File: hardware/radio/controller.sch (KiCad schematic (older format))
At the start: 11 parts, among them IC301 ATMEGA328-P, Q301 Q_NMOS_DGS, X301 8MHz

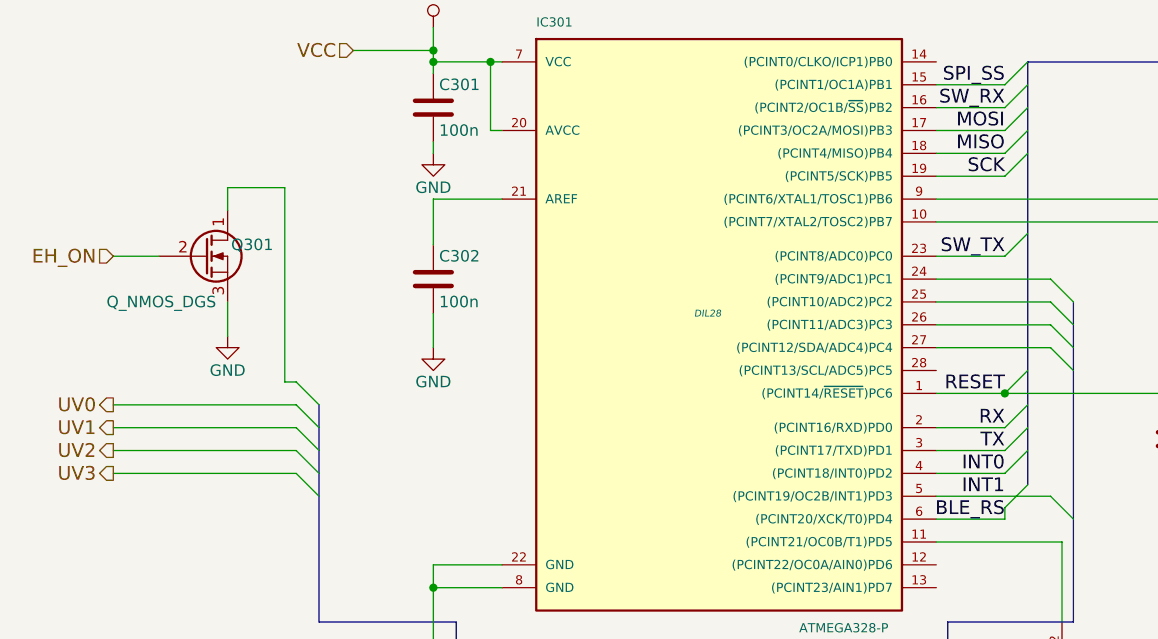
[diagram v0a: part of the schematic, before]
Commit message: Add accelerometer to schematic
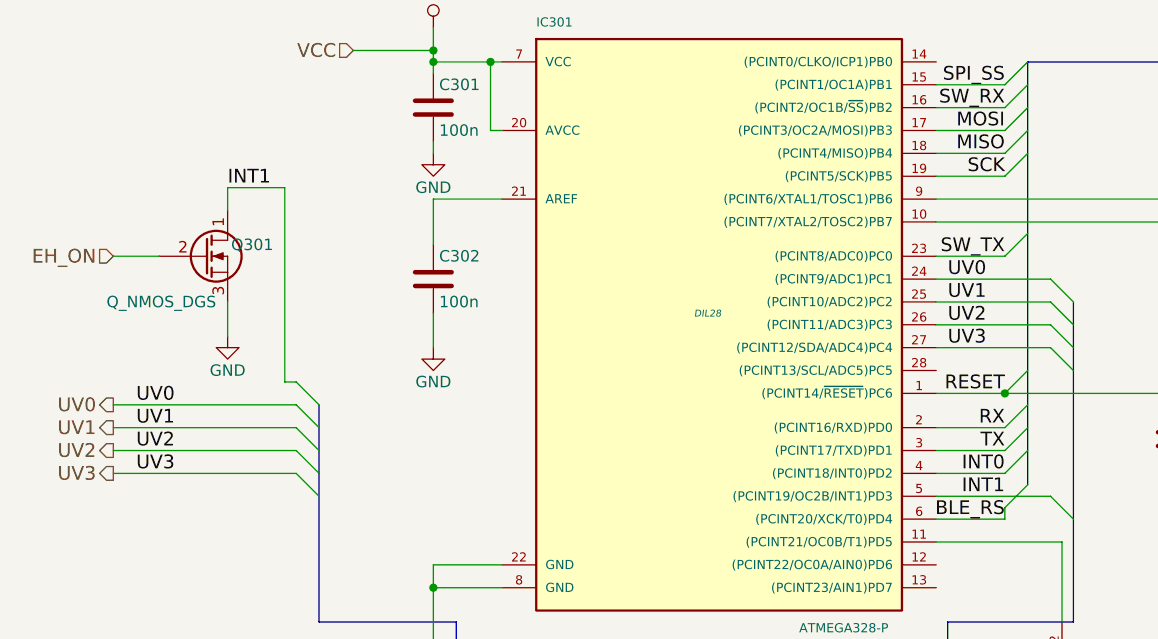
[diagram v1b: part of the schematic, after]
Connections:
- net INT1: now also Q301.1 (D)
- net UV0: now also IC301.24 ((PCINT9/ADC1)PC1)
- net UV1: now also IC301.25 ((PCINT10/ADC2)PC2)
- net UV2: now also IC301.26 ((PCINT11/ADC3)PC3)
- net UV3: now also IC301.27 ((PCINT12/SDA/ADC4)PC4)
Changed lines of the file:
@@
 LIBS:sensors
 LIBS:rfcom
+LIBS:radio-cache
 EELAYER 25 0
 EELAYER END
@@
 $EndComp
 $Comp
-L GND #PWR026
+L GND #PWR308
 U 1 1 55EA8C66
 P 7600 3250
-F 0 "#PWR026" H 7600 3000 50  0001 C CNN
+F 0 "#PWR308" H 7600 3000 50  0001 C CNN
 F 1 "GND" H 7600 3100 50  0000 C CNN
 F 2 "" H 7600 3250 60  0000 C CNN
@@
 $EndComp
 $Comp
-L GND #PWR027
+L GND #PWR307
 U 1 1 55EA8C82
 P 7300 3250
-F 0 "#PWR027" H 7300 3000 50  0001 C CNN
+F 0 "#PWR307" H 7300 3000 50  0001 C CNN
 F 1 "GND" H 7300 3100 50  0000 C CNN
 F 2 "" H 7300 3250 60  0000 C CNN
@@
 $EndComp
 $Comp
-L GND #PWR028
+L GND #PWR306
 U 1 1 55EA8C9E
 P 7000 3250
-F 0 "#PWR028" H 7000 3000 50  0001 C CNN
+F 0 "#PWR306" H 7000 3000 50  0001 C CNN
 F 1 "GND" H 7000 3100 50  0000 C CNN
 F 2 "" H 7000 3250 60  0000 C CNN
@@
 $EndComp
 $Comp
-L VCC #PWR029
+L VCC #PWR303
 U 1 1 55EA9129
 P 6450 3050
-F 0 "#PWR029" H 6450 2900 50  0001 C CNN
+F 0 "#PWR303" H 6450 2900 50  0001 C CNN
 F 1 "VCC" H 6450 3200 50  0000 C CNN
 F 2 "" H 6450 3050 60  0000 C CNN
@@
 $EndComp
 $Comp
-L GND #PWR030
+L GND #PWR309
 U 1 1 55EA91E9
 P 6450 3850
-F 0 "#PWR030" H 6450 3600 50  0001 C CNN
+F 0 "#PWR309" H 6450 3600 50  0001 C CNN
 F 1 "GND" H 6450 3700 50  0000 C CNN
 F 2 "" H 6450 3850 60  0000 C CNN
@@
 TX
 $Comp
-L GND #PWR031
+L GND #PWR310
 U 1 1 55EA9D7E
 P 3200 4750
-F 0 "#PWR031" H 3200 4500 50  0001 C CNN
+F 0 "#PWR310" H 3200 4500 50  0001 C CNN
 F 1 "GND" H 3200 4600 50  0000 C CNN
 F 2 "" H 3200 4750 60  0000 C CNN
@@
 $EndComp
 $Comp
-L GND #PWR032
+L GND #PWR305
 U 1 1 55EA9F10
 P 3200 3250
-F 0 "#PWR032" H 3200 3000 50  0001 C CNN
+F 0 "#PWR305" H 3200 3000 50  0001 C CNN
 F 1 "GND" H 3200 3100 50  0000 C CNN
 F 2 "" H 3200 3250 60  0000 C CNN
@@
 $EndComp
 $Comp
-L VCC #PWR033
+L VCC #PWR301
 U 1 1 55EAA1EE
 P 3200 1850
-F 0 "#PWR033" H 3200 1700 50  0001 C CNN
+F 0 "#PWR301" H 3200 1700 50  0001 C CNN
 F 1 "VCC" H 3200 2000 50  0000 C CNN
 F 2 "" H 3200 1850 60  0000 C CNN
@@
 $EndComp
 $Comp
-L GND #PWR034
+L GND #PWR302
 U 1 1 55EAA376
 P 3200 2400
-F 0 "#PWR034" H 3200 2150 50  0001 C CNN
+F 0 "#PWR302" H 3200 2150 50  0001 C CNN
 F 1 "GND" H 3200 2250 50  0000 C CNN
 F 2 "" H 3200 2400 60  0000 C CNN
@@
 $EndComp
 $Comp
-L GND #PWR035
+L GND #PWR311
 U 1 1 55EACDAA
 P 5950 5400
-F 0 "#PWR035" H 5950 5150 50  0001 C CNN
+F 0 "#PWR311" H 5950 5150 50  0001 C CNN
 F 1 "GND" H 5950 5250 50  0000 C CNN
 F 2 "" H 5950 5400 60  0000 C CNN
@@
 $EndComp
 $Comp
-L GND #PWR036
+L GND #PWR304
 U 1 1 55EAF28A
 P 2300 3200
-F 0 "#PWR036" H 2300 2950 50  0001 C CNN
+F 0 "#PWR304" H 2300 2950 50  0001 C CNN
 F 1 "GND" H 2300 3050 50  0000 C CNN
 F 2 "" H 2300 3200 60  0000 C CNN
@@
 Text Label 9450 900  2    60   ~ 0
 BLE_RS
+Text Label 2300 2550 0    60   ~ 0
+INT1
+Text Label 1900 3500 0    60   ~ 0
+UV0
+Text Label 1900 3600 0    60   ~ 0
+UV1
+Text Label 1900 3700 0    60   ~ 0
+UV2
+Text Label 1900 3800 0    60   ~ 0
+UV3
+Text Label 5450 2950 0    60   ~ 0
+UV0
+Text Label 5450 3050 0    60   ~ 0
+UV1
+Text Label 5450 3150 0    60   ~ 0
+UV2
+Text Label 5450 3250 0    60   ~ 0
+UV3
 $EndSCHEMATC

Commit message: Work on PCB
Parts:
- removed IC301: ATMEGA328-P, DIL28, symbol ATMEGA328-P
- added C?: C, symbol C
- added IC?: ATMEGA328-A, TQFP32, symbol ATMEGA328-A
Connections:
- net BLE_RS: now also IC?.2 ((PCINT20/XCK/T0)PD4)
- net GND: now also C?.2, IC?.21 (GND), IC?.3 (GND), IC?.5 (GND)
- net INT0: now also IC?.32 ((PCINT18/INT0)PD2)
- net INT1: now also IC?.1 ((PCINT19/OC2B/INT1)PD3)
- net MISO: now also IC?.16 ((PCINT4/MISO)PB4)
- net MOSI: now also IC?.15 ((PCINT3/OC2A/MOSI)PB3)
- net RESET: now also IC?.29 ((PCINT14/~RESET~)PC6)
- net RX: now also IC?.30 ((PCINT16/RXD)PD0)
- net SCK: now also IC?.17 ((PCINT5/SCK)PB5)
- net SPI_SS: now also IC?.13 ((PCINT1/OC1A)PB1)
- net SW_RX: now also IC?.14 ((PCINT2/OC1B/~SS~)PB2)
- net SW_TX: now also IC?.23 ((PCINT8/ADC0)PC0)
- net TX: now also IC?.31 ((PCINT17/TXD)PD1)
- net UV0: now also IC?.24 ((PCINT9/ADC1)PC1)
- net UV1: now also IC?.25 ((PCINT10/ADC2)PC2)
- net UV2: now also IC?.26 ((PCINT11/ADC3)PC3)
- net UV3: now also IC?.27 ((PCINT12/SDA/ADC4)PC4)
- net VCC: now also C?.1, IC?.18 (AVCC), IC?.4 (VCC), IC?.6 (VCC)
- net at C304.1, X301.2: now also IC?.8 ((PCINT7/XTAL2/TOSC2)PB7)
- net at D301.2 (A): now also IC?.9 ((PCINT21/OC0B/T1)PD5)
- net at C302.1: now also IC?.20 (AREF)
- net at C303.1, X301.1: now also IC?.7 ((PCINT6/XTAL1/TOSC1)PB6)
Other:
- moved on the sheet: C301
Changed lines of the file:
@@
 $EndDescr
-$Comp
-L ATMEGA328-P IC301
-U 1 1 55EA8691
-P 4400 3100
-F 0 "IC301" H 3650 4350 40  0000 L BNN
-F 1 "ATMEGA328-P" H 4800 1700 40  0000 L BNN
-F 2 "DIL28" H 4400 3100 30  0000 C CIN
-F 3 "" H 4400 3100 60  0000 C CNN
-	1    4400 3100
-	1    0    0    -1
-$EndComp
 $Comp
 L CRYSTAL_SMD X301
@@
 $EndComp
 $Comp
-L GND #PWR308
+L GND #PWR028
 U 1 1 55EA8C66
 P 7600 3250
-F 0 "#PWR308" H 7600 3000 50  0001 C CNN
+F 0 "#PWR028" H 7600 3000 50  0001 C CNN
 F 1 "GND" H 7600 3100 50  0000 C CNN
 F 2 "" H 7600 3250 60  0000 C CNN
@@
 $EndComp
 $Comp
-L GND #PWR307
+L GND #PWR029
 U 1 1 55EA8C82
 P 7300 3250
-F 0 "#PWR307" H 7300 3000 50  0001 C CNN
+F 0 "#PWR029" H 7300 3000 50  0001 C CNN
 F 1 "GND" H 7300 3100 50  0000 C CNN
 F 2 "" H 7300 3250 60  0000 C CNN
@@
 $EndComp
 $Comp
-L GND #PWR306
+L GND #PWR030
 U 1 1 55EA8C9E
 P 7000 3250
-F 0 "#PWR306" H 7000 3000 50  0001 C CNN
+F 0 "#PWR030" H 7000 3000 50  0001 C CNN
 F 1 "GND" H 7000 3100 50  0000 C CNN
 F 2 "" H 7000 3250 60  0000 C CNN
@@
 $EndComp
 $Comp
-L VCC #PWR303
+L VCC #PWR031
 U 1 1 55EA9129
 P 6450 3050
-F 0 "#PWR303" H 6450 2900 50  0001 C CNN
+F 0 "#PWR031" H 6450 2900 50  0001 C CNN
 F 1 "VCC" H 6450 3200 50  0000 C CNN
 F 2 "" H 6450 3050 60  0000 C CNN
@@
 $EndComp
 $Comp
-L GND #PWR309
+L GND #PWR032
 U 1 1 55EA91E9
 P 6450 3850
-F 0 "#PWR309" H 6450 3600 50  0001 C CNN
+F 0 "#PWR032" H 6450 3600 50  0001 C CNN
 F 1 "GND" H 6450 3700 50  0000 C CNN
 F 2 "" H 6450 3850 60  0000 C CNN
@@
 TX
 $Comp
-L GND #PWR310
+L GND #PWR033
 U 1 1 55EA9D7E
 P 3200 4750
-F 0 "#PWR310" H 3200 4500 50  0001 C CNN
+F 0 "#PWR033" H 3200 4500 50  0001 C CNN
 F 1 "GND" H 3200 4600 50  0000 C CNN
 F 2 "" H 3200 4750 60  0000 C CNN
@@
 $EndComp
 $Comp
-L GND #PWR305
+L GND #PWR034
 U 1 1 55EA9F10
 P 3200 3250
-F 0 "#PWR305" H 3200 3000 50  0001 C CNN
+F 0 "#PWR034" H 3200 3000 50  0001 C CNN
 F 1 "GND" H 3200 3100 50  0000 C CNN
 F 2 "" H 3200 3250 60  0000 C CNN
@@
 $EndComp
 $Comp
-L VCC #PWR301
+L VCC #PWR035
 U 1 1 55EAA1EE
-P 3200 1850
-F 0 "#PWR301" H 3200 1700 50  0001 C CNN
-F 1 "VCC" H 3200 2000 50  0000 C CNN
-F 2 "" H 3200 1850 60  0000 C CNN
-F 3 "" H 3200 1850 60  0000 C CNN
-	1    3200 1850
+P 2900 1850
+F 0 "#PWR035" H 2900 1700 50  0001 C CNN
+F 1 "VCC" H 2900 2000 50  0000 C CNN
+F 2 "" H 2900 1850 60  0000 C CNN
+F 3 "" H 2900 1850 60  0000 C CNN
+	1    2900 1850
 	1    0    0    -1
 $EndComp
@@
 L C C301
 U 1 1 55EAA2CA
-P 3200 2200
-F 0 "C301" H 3225 2300 50  0000 L CNN
-F 1 "100n" H 3225 2100 50  0000 L CNN
-F 2 "" H 3238 2050 30  0000 C CNN
-F 3 "" H 3200 2200 60  0000 C CNN
-	1    3200 2200
-	1    0    0    -1
-$EndComp
-$Comp
-L GND #PWR302
+P 2900 2200
+F 0 "C301" H 2925 2300 50  0000 L CNN
+F 1 "100n" H 2925 2100 50  0000 L CNN
+F 2 "" H 2938 2050 30  0000 C CNN
+F 3 "" H 2900 2200 60  0000 C CNN
+	1    2900 2200
+	1    0    0    -1
+$EndComp
+$Comp
+L GND #PWR036
 U 1 1 55EAA376
-P 3200 2400
-F 0 "#PWR302" H 3200 2150 50  0001 C CNN
-F 1 "GND" H 3200 2250 50  0000 C CNN
-F 2 "" H 3200 2400 60  0000 C CNN
-F 3 "" H 3200 2400 60  0000 C CNN
-	1    3200 2400
+P 2900 2400
+F 0 "#PWR036" H 2900 2150 50  0001 C CNN
+F 1 "GND" H 2900 2250 50  0000 C CNN
+F 2 "" H 2900 2400 60  0000 C CNN
+F 3 "" H 2900 2400 60  0000 C CNN
+	1    2900 2400
 	1    0    0    -1
 $EndComp
@@
 Text HLabel 2850 4650 0    60   Input ~ 0
 GND
-Text HLabel 2850 1950 0    60   Input ~ 0
+Text HLabel 2550 1950 0    60   Input ~ 0
 VCC
 $Comp
@@
 $EndComp
 $Comp
-L GND #PWR311
+L GND #PWR037
 U 1 1 55EACDAA
 P 5950 5400
-F 0 "#PWR311" H 5950 5150 50  0001 C CNN
+F 0 "#PWR037" H 5950 5150 50  0001 C CNN
 F 1 "GND" H 5950 5250 50  0000 C CNN
 F 2 "" H 5950 5400 60  0000 C CNN
@@
 $EndComp
 $Comp
-L GND #PWR304
+L GND #PWR038
 U 1 1 55EAF28A
 P 2300 3200
-F 0 "#PWR304" H 2300 2950 50  0001 C CNN
+F 0 "#PWR038" H 2300 2950 50  0001 C CNN
 F 1 "GND" H 2300 3050 50  0000 C CNN
 F 2 "" H 2300 3200 60  0000 C CNN
@@
 	3500 4200 3200 4200
 Wire Wire Line
-	3200 4200 3200 4750
+	3200 4100 3200 4750
 Wire Wire Line
 	3500 4300 3200 4300
 Connection ~ 3200 4300
 Wire Wire Line
-	3500 2300 3450 2300
-Wire Wire Line
-	3450 2300 3450 2000
-Wire Wire Line
-	3200 2000 3500 2000
+	3450 2300 3500 2300
+Wire Wire Line
+	3450 2000 3450 2300
+Wire Wire Line
+	2900 2000 3500 2000
 Connection ~ 3450 2000
 Wire Wire Line
@@
 	3200 3100 3200 3250
 Wire Wire Line
-	3200 1850 3200 2050
-Connection ~ 3200 2000
-Wire Wire Line
-	3200 2350 3200 2400
+	2900 1850 2900 2050
+Connection ~ 2900 2000
+Wire Wire Line
+	2900 2350 2900 2400
 Wire Bus Line
 	9050 1000 9050 2000
@@
 	9150 1900 9550 1900
 Wire Wire Line
-	3200 1950 2850 1950
-Connection ~ 3200 1950
+	2900 1950 2550 1950
+Connection ~ 2900 1950
 Wire Wire Line
 	3200 4650 2850 4650
@@
 Text Label 5450 3250 0    60   ~ 0
 UV3
+$Comp
+L ATMEGA328-A IC?
+U 1 1 55ED2326
+P 4400 3100
+F 0 "IC?" H 3650 4350 40  0000 L BNN
+F 1 "ATMEGA328-A" H 4800 1700 40  0000 L BNN
+F 2 "TQFP32" H 4400 3100 30  0000 C CIN
+F 3 "" H 4400 3100 60  0000 C CNN
+	1    4400 3100
+	1    0    0    -1
+$EndComp
+Wire Wire Line
+	3500 2100 3450 2100
+Connection ~ 3450 2100
+Wire Wire Line
+	3500 4100 3200 4100
+Connection ~ 3200 4200
+$Comp
+L C C?
+U 1 1 55ED2949
+P 3250 2200
+F 0 "C?" H 3275 2300 50  0000 L CNN
+F 1 "C" H 3275 2100 50  0000 L CNN
+F 2 "" H 3288 2050 30  0000 C CNN
+F 3 "" H 3250 2200 60  0000 C CNN
+	1    3250 2200
+	1    0    0    -1
+$EndComp
+Wire Wire Line
+	3250 2000 3250 2050
+Connection ~ 3250 2000
+Wire Wire Line
+	3250 2350 3250 2400
+$Comp
+L GND #PWR?
+U 1 1 55ED2A96
+P 3250 2400
+F 0 "#PWR?" H 3250 2150 50  0001 C CNN
+F 1 "GND" H 3250 2250 50  0000 C CNN
+F 2 "" H 3250 2400 60  0000 C CNN
+F 3 "" H 3250 2400 60  0000 C CNN
+	1    3250 2400
+	1    0    0    -1
+$EndComp
 $EndSCHEMATC

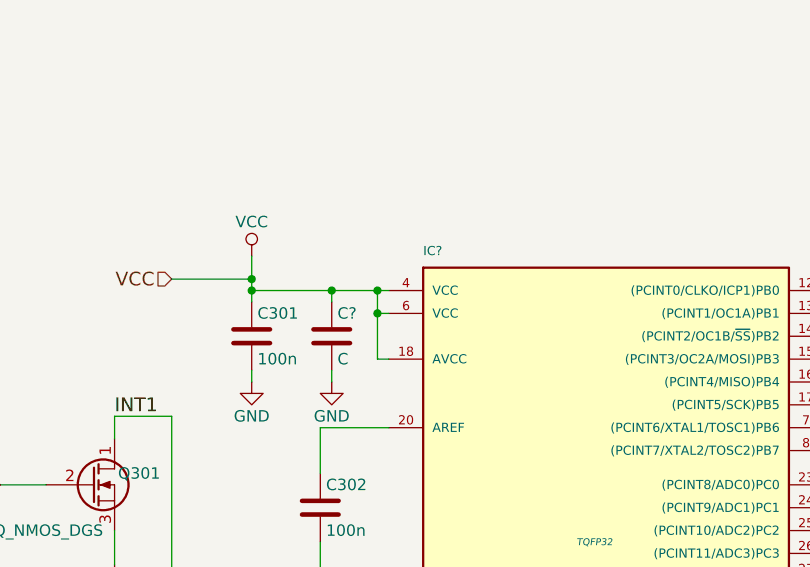
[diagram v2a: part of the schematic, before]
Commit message: Fix the µC part number, pin numbering
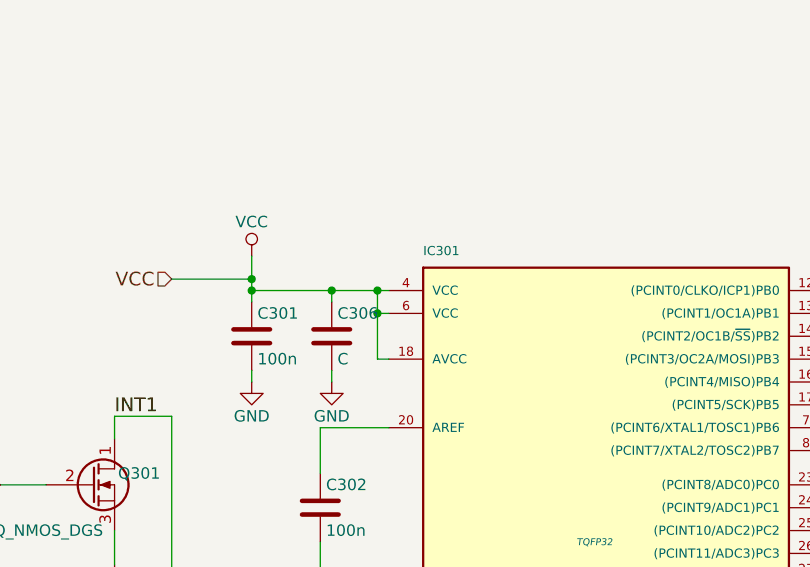
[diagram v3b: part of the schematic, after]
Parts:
- gave numbers to parts that had none: 2
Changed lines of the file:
@@
 UV3
 $Comp
-L ATMEGA328-A IC?
+L ATMEGA328-A IC301
 U 1 1 55ED2326
 P 4400 3100
-F 0 "IC?" H 3650 4350 40  0000 L BNN
+F 0 "IC301" H 3650 4350 40  0000 L BNN
 F 1 "ATMEGA328-A" H 4800 1700 40  0000 L BNN
 F 2 "TQFP32" H 4400 3100 30  0000 C CIN
@@
 Connection ~ 3200 4200
 $Comp
-L C C?
+L C C306
 U 1 1 55ED2949
 P 3250 2200
-F 0 "C?" H 3275 2300 50  0000 L CNN
+F 0 "C306" H 3275 2300 50  0000 L CNN
 F 1 "C" H 3275 2100 50  0000 L CNN
 F 2 "" H 3288 2050 30  0000 C CNN
@@
 	3250 2350 3250 2400
 $Comp
-L GND #PWR?
+L GND #PWR039
 U 1 1 55ED2A96
 P 3250 2400
-F 0 "#PWR?" H 3250 2150 50  0001 C CNN
+F 0 "#PWR039" H 3250 2150 50  0001 C CNN
 F 1 "GND" H 3250 2250 50  0000 C CNN
 F 2 "" H 3250 2400 60  0000 C CNN
